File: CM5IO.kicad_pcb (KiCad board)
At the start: 4 copper layers, 160 x 90 mm, 76 parts, among them J10 690-019-298-412, J11 USB_C_Receptacle_USB2.0, J12 USB3_A, J14 JST_SHBM04B-SRSS-TB, J16 Conn_01x22_Female, J2 Conn_02x07_Odd_Even, J22 690-019-298-412, J3 Conn_01x03, J4 Bus_M.2_Socket_M, J5 Conn_01x22_Female, J6 THD-02-R, J7 Micro_SD_Card_Det, J8 THD-20-R, J9 THD-02-R, SW1 Right angle Tact button, U1 TPD4EUSB30, U12 RT9742SNGV, U18 RT9742GGJ5, U2 TPD4EUSB30, U3 MagJack-A70-112-331N126, U5 74LVC1G07SE-7, U6 AP22653W6, U7 ASEK-32.768KHZ-L-R-T, U8 AP3441SHE-7B

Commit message: first pass at layout
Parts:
- removed C10, C19: 100n, Capacitor_SMD:C_0402_1005Metric
- removed C11: 4.7nF, Capacitor_SMD:C_0402_1005Metric
- removed C14, C15, C16, C17, C4, C6: 10u, Capacitor_SMD:C_0805_2012Metric
- removed L1: 2.2uH, CM5IO:L_Bourns_SRP5030CC
- removed R14: 100K 1%, Resistor_SMD:R_0402_1005Metric
- removed R15: 10K 1%, Resistor_SMD:R_0402_1005Metric
- removed R16: 2.2K 1%, Resistor_SMD:R_0402_1005Metric
- removed R17: 1k, Resistor_SMD:R_0402_1005Metric
- removed TP1: TestPoint, TestPoint:TestPoint_Pad_2.0x2.0mm
- removed U7: ASEK-32.768KHZ-L-R-T, Crystal:Crystal_SMD_3225-4Pin_3.2x2.5mm
- removed U8: AP3441SHE-7B, Package_DFN_QFN:DFN-8-1EP_2x2mm_P0.5mm_EP1.05x1.75mm
- added J1: PCIE-164-02-F-D-TH, CM5IO:CONN_PCIE-164-02-x-D-TH_SAI, F.Cu at (182.8, 187.7)
- added J13: THD-02-R, Connector_PinHeader_2.54mm:PinHeader_2x02_P2.54mm_Vertical, F.Cu at (97.0, 194.0)
- added Q1: BS170F, Package_TO_SOT_SMD:SOT-23, F.Cu at (56.3, 78.8)
- added R11: 1k, Resistor_SMD:R_0402_1005Metric, F.Cu at (96.7, 199.8)
- added R13: 1k, Resistor_SMD:R_0402_1005Metric, F.Cu at (94.0, 197.5)
- D3: value LED Green -> D; footprint LED_SMD:LED_0603_1608Metric -> Diode_SMD:D_SOD-323F
- H1, H6, H7, H8: footprint CM5IO:MountingHole_2.7mm_M2.5_DIN965 -> CM5IO:atx_mountinghole
- J4: value Bus_M.2_Socket_M -> ATX-24; footprint CM5IO:M.2 M Key socket -> Connector_Molex:Molex_Mini-Fit_Jr_5566-24A_2x12_P4.20mm_Vertical
- moved J4 199.4 mm to (46.6, 66.3), turned to 0 degrees
- moved D3 171.3 mm to (60.5, 78.0), turned to 90 degrees
- moved J8 89.2 mm to (30.9, 177.8)
- moved C1 89.2 mm to (95.8, 207.3)
- moved J9 89.2 mm to (85.3, 220.8)
- moved R3 89.2 mm to (103.8, 207.2)
- moved TP3 89.2 mm to (59.9, 225.1)
- moved C12 89.2 mm to (55.0, 218.5)
- moved C13 89.2 mm to (60.3, 217.6)
- moved C18 89.2 mm to (133.7, 220.1)
- moved C2 89.2 mm to (131.9, 198.7)
- moved C3 89.2 mm to (129.4, 210.6)
- moved C5 89.2 mm to (142.9, 212.8)
- moved C7 89.2 mm to (113.7, 210.9)
- moved C8 89.2 mm to (113.6, 208.5)
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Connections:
- net Net-(Module1A-LED_nACT) renamed /CM5_GPIO ( Ethernet, GPIO, SDCARD)/LED_nACT
- D3 pad 1: Net-(D3-K) -> /PWR_BUT
- D3 pad 2: /PCIe-M2/M2_3v3 -> Net-(D3-A)
- J2 pad 14: /CM5_GPIO ( Ethernet, GPIO, SDCARD)/PWR_BUT -> /PWR_BUT
- J4 pad 1: GND -> /+3.3v_pcie
- J4 pad 10: Net-(J4-DAS/~{DSS}/~{LED1}) -> /+12v
- J4 pad 11: unconnected-(J4-PERn3-Pad11) -> /+12v
- J4 pad 12: /PCIe-M2/M2_3v3 -> /+3.3v_pcie
- J4 pad 13: unconnected-(J4-PERp3-Pad13) -> /+3.3v_pcie
- J4 pad 14: /PCIe-M2/M2_3v3 -> unconnected-(J4--12V-Pad14)
- J4 pad 16: /PCIe-M2/M2_3v3 -> Net-(D3-A)
- J4 pad 17: unconnected-(J4-PETn2-Pad17) -> GND
- J4 pad 18: /PCIe-M2/M2_3v3 -> GND
- J4 pad 19: unconnected-(J4-PETp2-Pad19) -> GND
- J4 pad 2: /PCIe-M2/M2_3v3 -> /+3.3v_pcie
- J4 pad 21: GND -> /+5v
- J4 pad 22: unconnected-(J4-NC-Pad22) -> /+5v
- J4 pad 23: unconnected-(J4-PERn2-Pad23) -> /+5v
- J4 pad 24: unconnected-(J4-NC-Pad24) -> GND
- J4 pad 4: /PCIe-M2/M2_3v3 -> /+5v
- J4 pad 5: unconnected-(J4-PETn3-Pad5) -> GND
- J4 pad 6: unconnected-(J4-NC-Pad6) -> /+5v
- J4 pad 7: unconnected-(J4-PETp3-Pad7) -> GND
- J4 pad 9: GND -> unconnected-(J4-+5VSB-Pad9)
- Module1 pad 106: /CM5_HighSpeed/PCIE_PWR_EN -> unconnected-(Module1B-PCIE_PWR_EN-Pad106)
- Module1 pad 92: /CM5_GPIO ( Ethernet, GPIO, SDCARD)/PWR_BUT -> /PWR_BUT
- SW1 pad 1: /CM5_GPIO ( Ethernet, GPIO, SDCARD)/PWR_BUT -> /PWR_BUT
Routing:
- net /+3.3v_pcie: track 0.00 -> 342.6 mm, vias 0 -> 3
- net /+12v: track 0.00 -> 187.4 mm
- net /PWR_BUT: track 0.00 -> 174.0 mm, vias 0 -> 2
- net /+5v: track 284.2 -> 450.5 mm
- net /+3.3v: track 324.6 -> 433.7 mm, vias 8 -> 11
- net /CM5_GPIO ( Ethernet, GPIO, SDCARD)/PWR_BUT: track 96.7 -> 0.00 mm, vias 2 -> 0
- net /CM5_HighSpeed/PCIE_PWR_EN: track 71.3 -> 0.00 mm, vias 2 -> 0
- net /PCIe-M2/M2_3v3: track 70.4 -> 0.00 mm, vias 3 -> 0
- net GND: track 766.8 -> 701.2 mm, vias 477 -> 487
- net Net-(R10-Pad2): track 2.22 -> 55.3 mm, vias 0 -> 2
- net Net-(J4-DAS/~{DSS}/~{LED1}): track 24.1 -> 0.00 mm
- net unconnected-(Module1B-PCIE_PWR_EN-Pad106): track 0.00 -> 22.1 mm, vias 0 -> 1
- net /CM5_HighSpeed/PCIE_TX_N: track 109.5 -> 130.3 mm, vias 2 -> 1
- net /CM5_HighSpeed/PCIE_TX_P: track 109.5 -> 130.1 mm, vias 2 -> 1
- net /CM5_HighSpeed/PCIE_nCLKREQ: track 92.1 -> 105.5 mm, vias 4 -> 3
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- removed copper zone on F.Cu, net /PCIe-M2/M2_3v3
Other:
- board size 160 x 90 mm -> 170 x 170 mm
- board text added: "+pwr -pwr"
- board text added: "act+ act-"
- board text removed: "M.2 M Key"

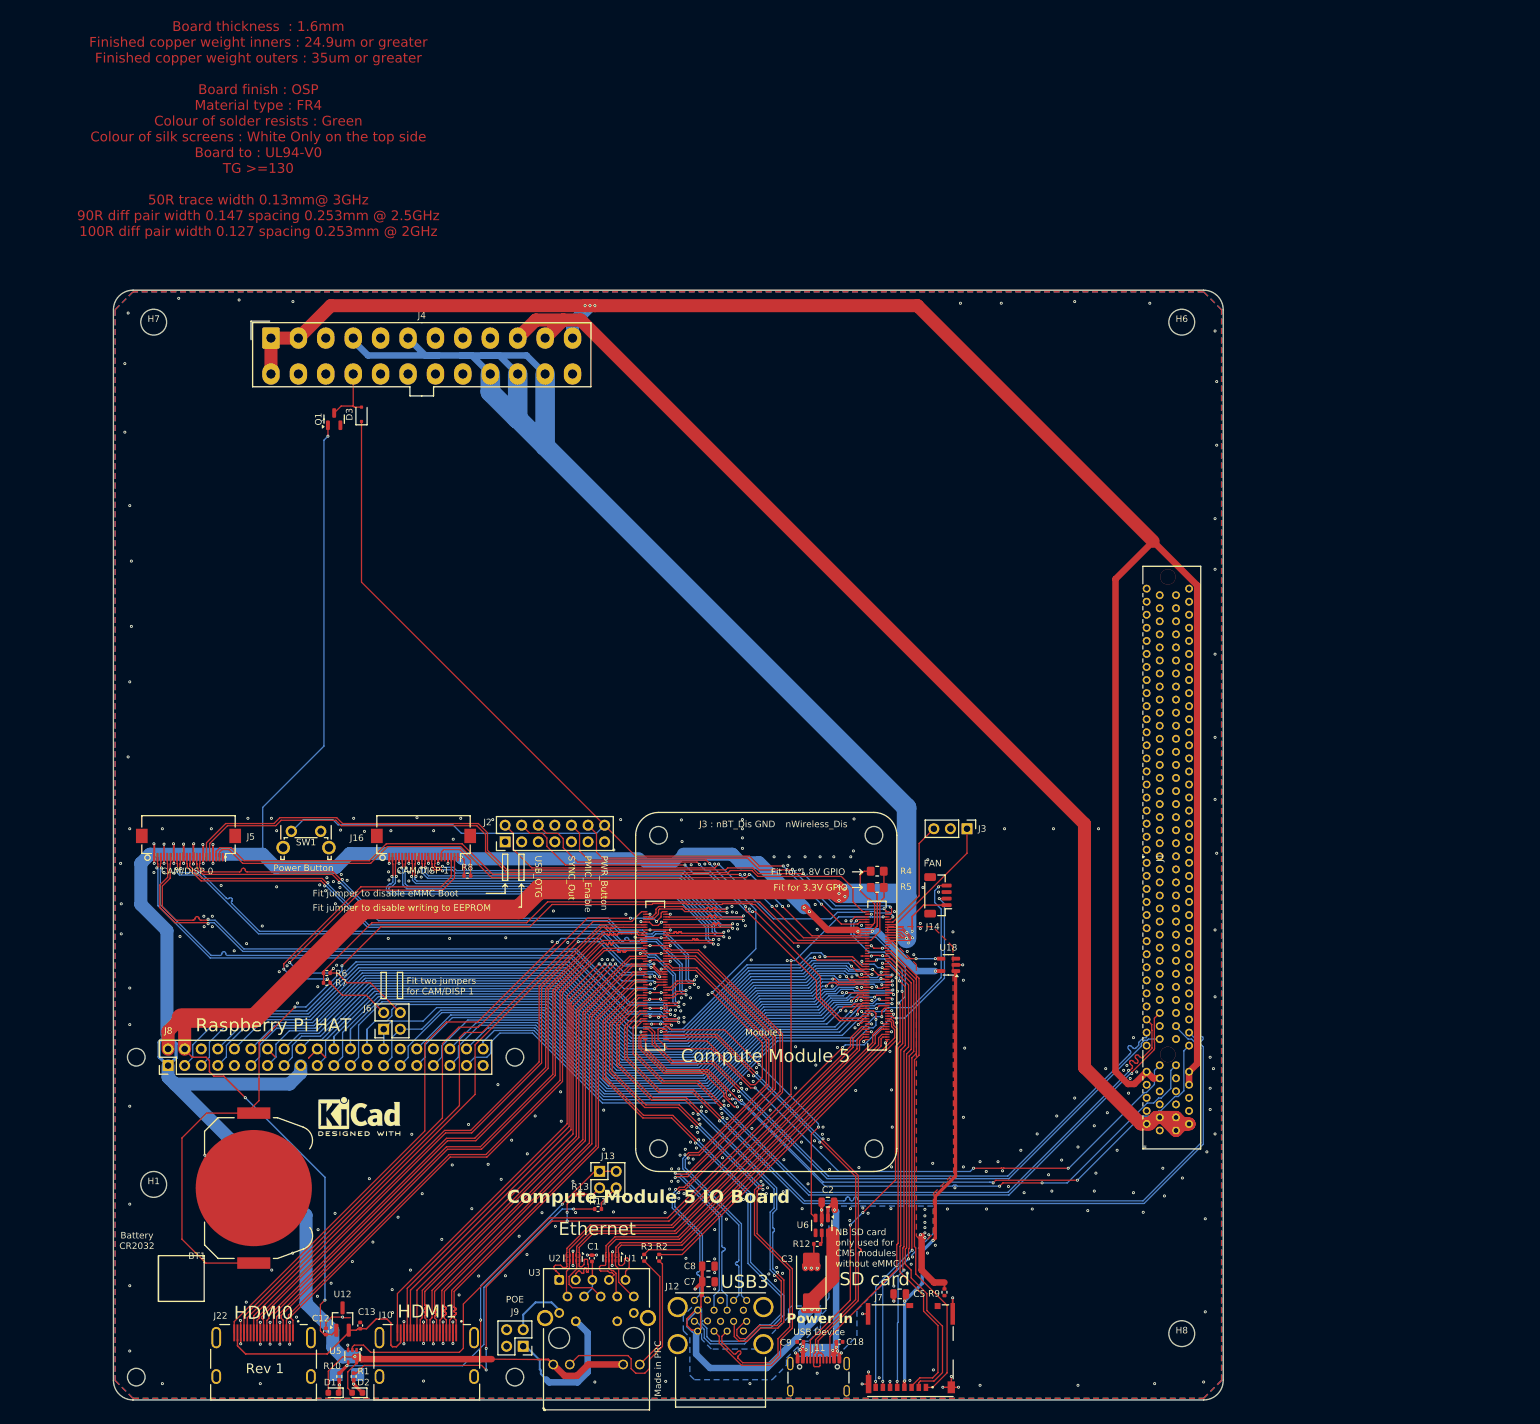
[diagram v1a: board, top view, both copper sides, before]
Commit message: fix PCIe position and PS_ON logic
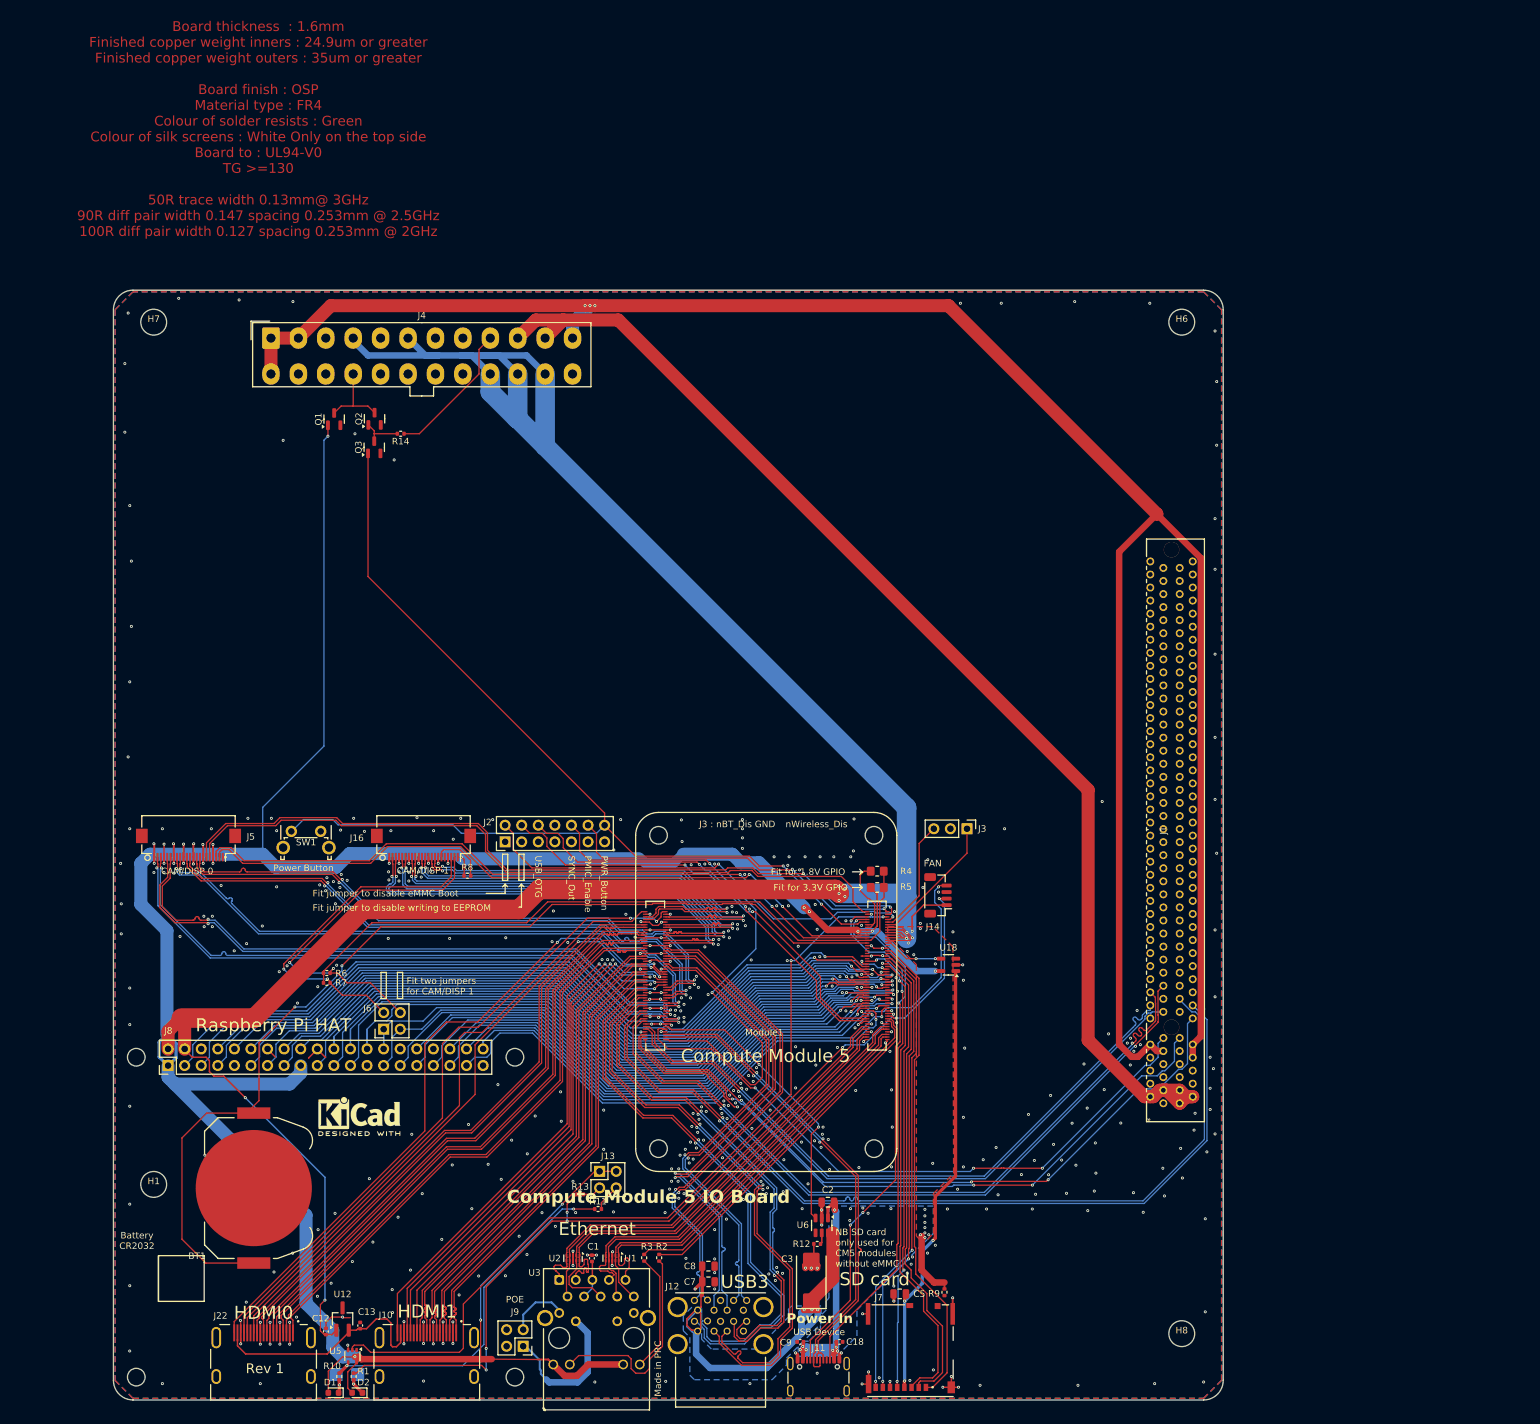
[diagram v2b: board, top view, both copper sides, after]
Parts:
- removed D3: D, Diode_SMD:D_SOD-323F
- added Q2: BS170F, Package_TO_SOT_SMD:SOT-23, F.Cu at (62.5, 78.7)
- added Q3: BS170F, Package_TO_SOT_SMD:SOT-23, F.Cu at (62.5, 83.1)
- added R14: 1k, Resistor_SMD:R_0402_1005Metric, F.Cu at (66.5, 81.0)
- moved J1 4.21 mm to (183.3, 183.5)
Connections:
- J4 pad 9: unconnected-(J4-+5VSB-Pad9) -> Net-(J4-+5VSB)
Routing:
- net Net-(J4-+5VSB): track 0.00 -> 21.5 mm
- net Net-(Q2-G): track 0.00 -> 6.40 mm
- net /PWR_BUT: track 174.0 -> 168.7 mm
- net /CM5_HighSpeed/PCIE_TX_N: track 130.3 -> 134.7 mm
- net /CM5_HighSpeed/PCIE_TX_P: track 130.1 -> 134.5 mm
- net Net-(J4-PS_ON#): track 9.63 -> 12.0 mm
- net /CM5_HighSpeed/PCIE_RX_P: track 110.6 -> 112.9 mm
- net /CM5_HighSpeed/PCIE_RX_N: track 110.8 -> 113.1 mm
- net /CM5_HighSpeed/PCIE_nRST: track 96.0 -> 98.3 mm
- net /CM5_HighSpeed/PCIE_CLK_P: track 98.5 -> 100.8 mm
- net /CM5_HighSpeed/PCIE_CLK_N: track 98.6 -> 100.9 mm
- net /CM5_HighSpeed/PCIE_nCLKREQ: track 105.5 -> 107.7 mm
- net /CM5_HighSpeed/PCIE_nWAKE: track 102.8 -> 104.9 mm
- net /+3.3v_pcie: track 342.6 -> 341.5 mm
- net /+12v: track 187.4 -> 186.8 mm
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
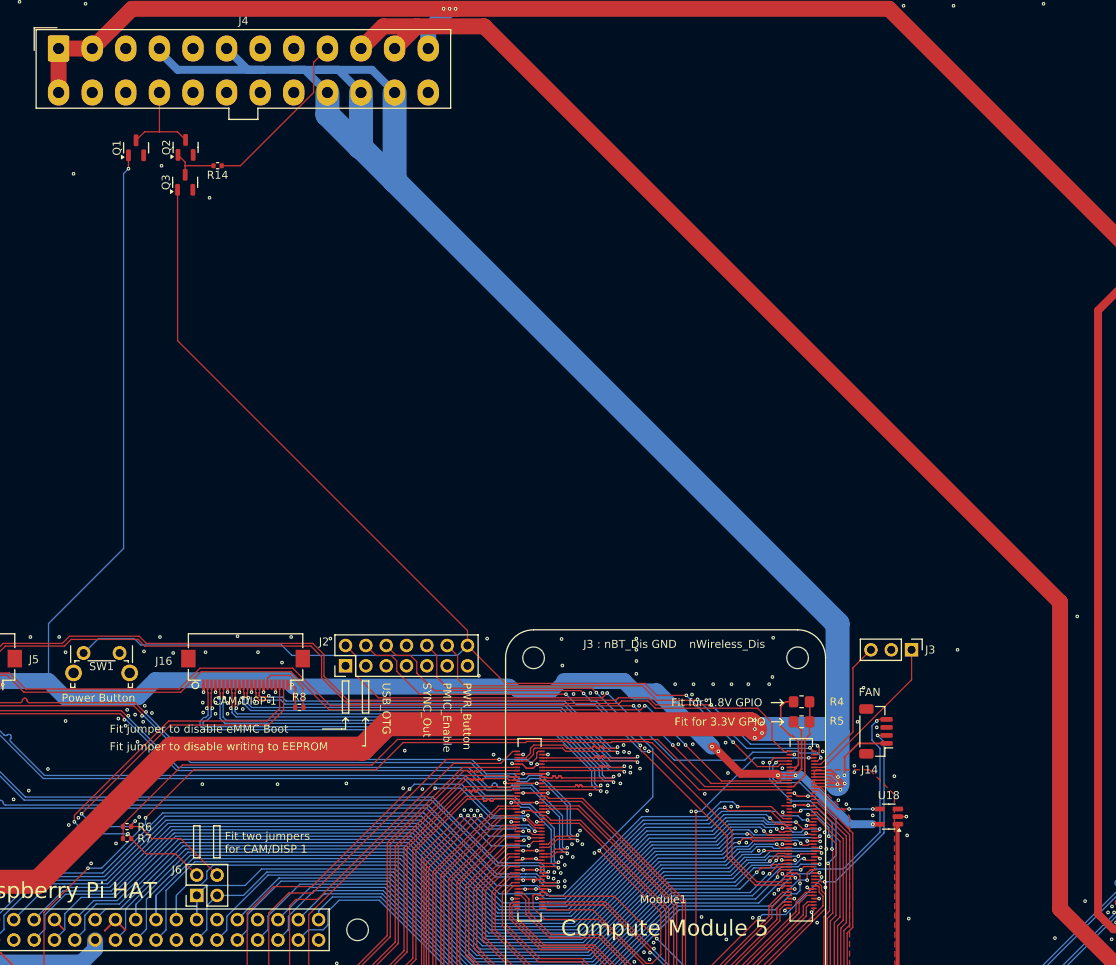
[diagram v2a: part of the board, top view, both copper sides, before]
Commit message: add LCSC part numbers, redo fan header and ps_on logic
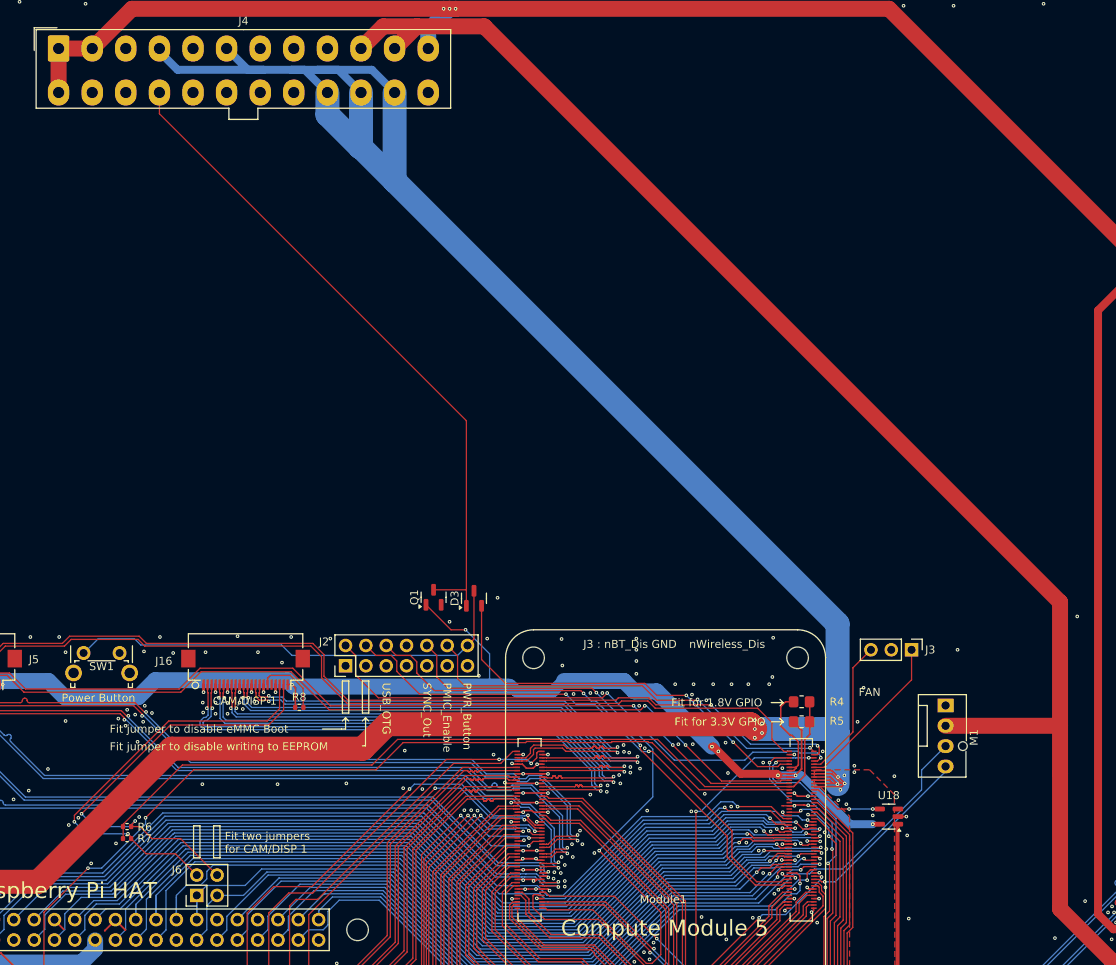
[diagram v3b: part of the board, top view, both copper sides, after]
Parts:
- removed J14: JST_SHBM04B-SRSS-TB, Connector_JST:JST_SH_BM04B-SRSS-TB_1x04-1MP_P1.00mm_Vertical
- removed Q2, Q3: BS170F, Package_TO_SOT_SMD:SOT-23
- removed R14: 1k, Resistor_SMD:R_0402_1005Metric
- added D3: D_Dual_CommonCathode_AAK, Package_TO_SOT_SMD:SOT-23, F.Cu at (98.5, 135.1)
- added M1: Fan_4pin, Connector:FanPinHeader_1x04_P2.54mm_Vertical, F.Cu at (157.5, 148.5)
- moved Q1 67.4 mm to (93.5, 134.9)
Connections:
- net Net-(J4-PS_ON#) renamed /CM5_GPIO ( Ethernet, GPIO, SDCARD)/PS_ON
- J2 pad 14: /PWR_BUT -> /CM5_GPIO ( Ethernet, GPIO, SDCARD)/PWR_BUT_RAW
- J4 pad 9: Net-(J4-+5VSB) -> unconnected-(J4-+5VSB-Pad9)
- Module1 pad 92: /PWR_BUT -> /CM5_GPIO ( Ethernet, GPIO, SDCARD)/PWR_BUT
- SW1 pad 1: /PWR_BUT -> /CM5_GPIO ( Ethernet, GPIO, SDCARD)/PWR_BUT_RAW
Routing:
- net /PWR_BUT: track 168.7 -> 0.00 mm, vias 2 -> 0
- net /CM5_GPIO ( Ethernet, GPIO, SDCARD)/PS_ON: track 12.0 -> 84.2 mm
- net /CM5_GPIO ( Ethernet, GPIO, SDCARD)/PWR_BUT_RAW: track 0.00 -> 57.3 mm
- net /+3.3v: track 433.7 -> 378.5 mm
- net /CM5_GPIO ( Ethernet, GPIO, SDCARD)/PWR_BUT: track 0.00 -> 50.8 mm, vias 0 -> 2
- net Net-(J4-+5VSB): track 21.5 -> 0.00 mm
- net /+12v: track 186.8 -> 201.1 mm
- net /+5v: track 450.5 -> 442.3 mm
- net Net-(Q2-G): track 6.40 -> 0.00 mm
- net /CM5_GPIO ( Ethernet, GPIO, SDCARD)/PWM: track 25.1 -> 22.9 mm, vias 2 -> 1
- net /CM5_GPIO ( Ethernet, GPIO, SDCARD)/TACHO: track 33.2 -> 31.4 mm, vias 2 -> 1
- net GND: vias 494 -> 492
